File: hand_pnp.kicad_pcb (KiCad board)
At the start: 2 copper layers, 46 x 41 mm, 17 parts, among them J1 Solenoid, J2 Motor, J3 12v in, J4 AudioJack3_Ground, Q1 FDN339AN, Q2 FDN339AN, SW1 power sw

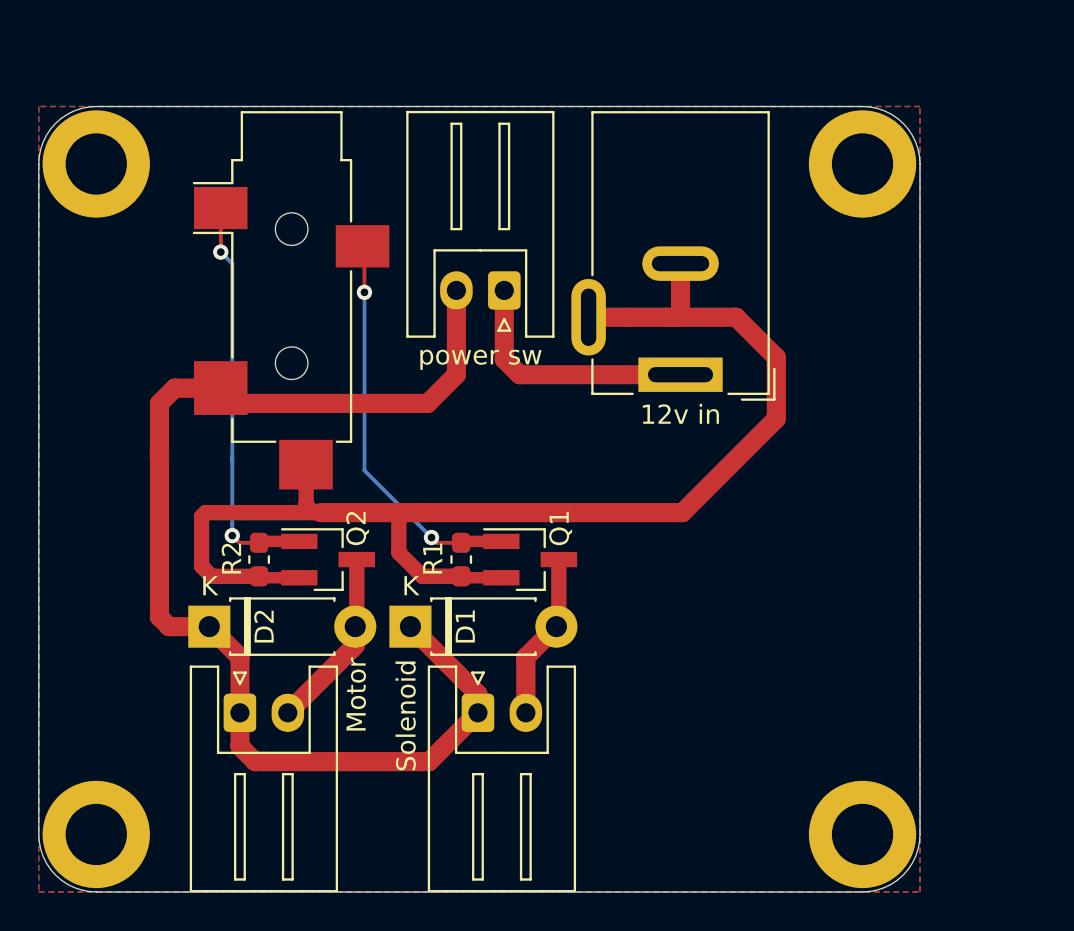
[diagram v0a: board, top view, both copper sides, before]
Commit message: Modified board to make it smaller
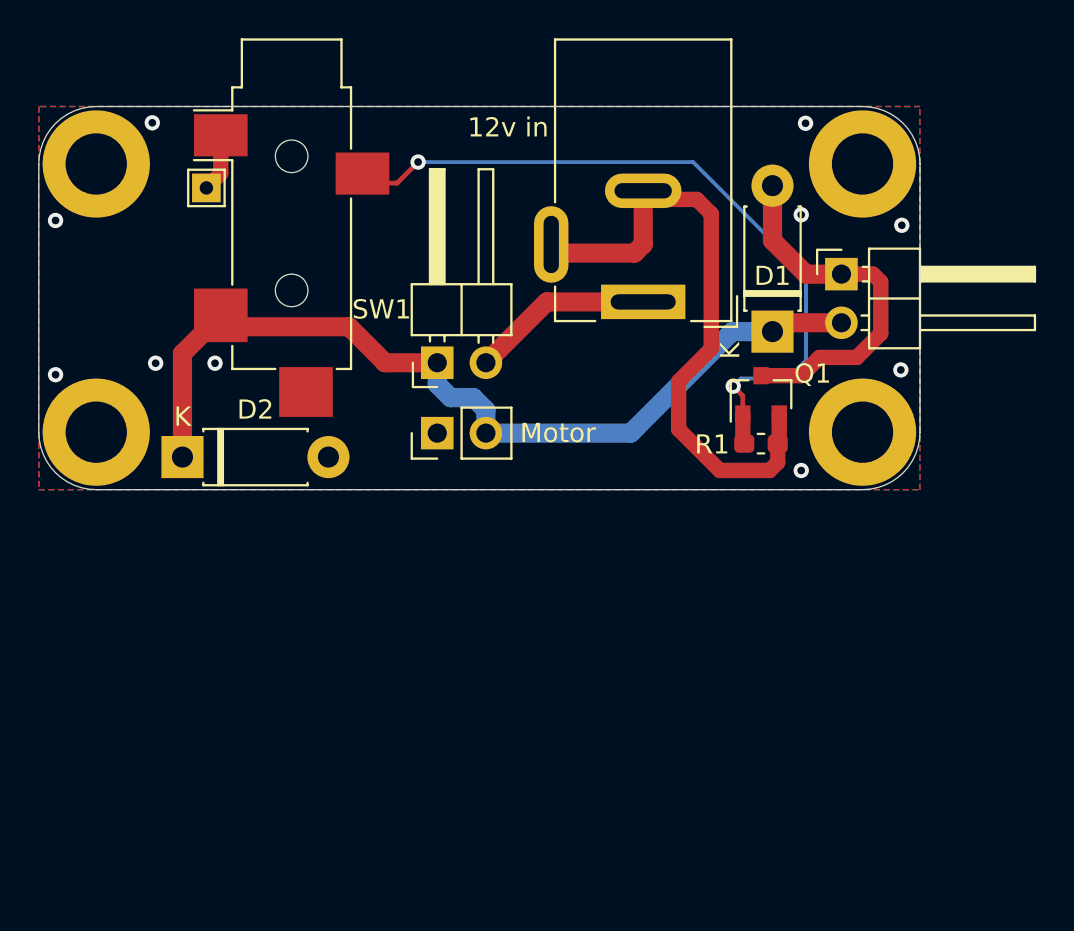
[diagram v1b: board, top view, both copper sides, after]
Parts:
- removed the G*** at (148.0, 49.0)
- removed the G*** at (159.9, 57.5)
- removed Q2: FDN339AN, Package_TO_SOT_SMD:SOT-23_Handsoldering
- removed R2: 10k, Resistor_SMD:R_0603_1608Metric_Pad1.05x0.95mm_HandSolder
- added G***: LOGO, graphics:kiwi10mm, F.Cu at (153.1, 45.5)
- added G***: LOGO, graphics:kiwi10mm, B.Cu at (135.2, 45.0)
- added J5: Motor, Connector_PinHeader_2.54mm:PinHeader_1x02_P2.54mm_Vertical, F.Cu at (143.8, 47.0)
- J1, SW1: footprint Connector_JST:JST_XH_S2B-XH-A_1x02_P2.50mm_Horizontal -> Connector_PinHeader_2.54mm:PinHeader_1x02_P2.54mm_Horizontal
- J2: value Motor -> pad; footprint Connector_JST:JST_XH_S2B-XH-A_1x02_P2.50mm_Horizontal -> TestPoint:TestPoint_THTPad_1.5x1.5mm_Drill0.7mm
- J4: value AudioJack3_Ground -> foot_switch
- Q1: footprint Package_TO_SOT_SMD:SOT-23_Handsoldering -> Package_TO_SOT_SMD:SOT-23
- moved J1 29.7 mm to (164.9, 38.8)
- moved J2 27.5 mm to (131.8, 34.2)
- moved D1 24.4 mm to (161.3, 41.8), turned to 90 degrees
- moved REF** 21.0 mm to (126.0, 47.0)
- moved REF** 21.0 mm to (166.0, 47.0)
- moved R1 16.8 mm to (160.7, 47.6), turned to 180 degrees
- moved Q1 14.8 mm to (160.7, 45.0), turned to 90 degrees
- moved D2 8.96 mm to (130.5, 48.3)
- moved SW1 5.15 mm to (143.8, 43.4), turned to 90 degrees
- moved J3 4.27 mm to (154.6, 40.2)
- moved J4 3.80 mm to (136.2, 35.1)
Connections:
- D2 pad 2: Net-(D2-Pad2) -> GND
- J1 pad 1: +12V -> Net-(D1-Pad2)
- J1 pad 2: Net-(D1-Pad2) -> +12V
- J2 pad 1: +12V -> Net-(J2-Pad1)
- J4 pad S: /motor_E -> Net-(J2-Pad1)
- SW1 pad 1: Net-(J3-Pad1) -> +12V
- SW1 pad 2: +12V -> Net-(J3-Pad1)
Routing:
- net GND: track 69.2 -> 31.9 mm, vias 0 -> 10
- net /motor_E: track 21.2 -> 0.00 mm, vias 2 -> 0
- net /solenoid_E: track 20.5 -> 38.1 mm
- net +12V: track 61.9 -> 46.3 mm
- net Net-(D1-Pad2): track 8.71 -> 19.3 mm
- net Net-(D2-Pad2): track 9.49 -> 0.00 mm
- net Net-(J3-Pad1): track 13.1 -> 9.53 mm
- net Net-(J2-Pad1): track 0.00 -> 3.06 mm
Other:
- board size 46 x 41 mm -> 46 x 20 mm
- net class Default: trace_width 0.25 -> 0.2
- board text added: "git.io/pnpglue"
- board text added: "v0.1"
- board text removed: "(3,3) (0,0)"
- board text removed: "(43,3) (40,0)"
- board text removed: "(43,38) ( 0,35)"
- board text removed: "(43,38) (40,35)"
- board text removed: "Mounting hole position is given in two ways (0,0) = top left board edge (0,0) = top left hole (seen from the top)"
